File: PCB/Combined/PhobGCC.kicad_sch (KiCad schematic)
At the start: 74 parts, among them J2 Conn_01x04_Female, J3 Conn_01x01_Male, J4 Conn_01x04_Male, J5 Conn_01x02_Male, Q1 Q_NMOS_GSD, Q2 Q_PMOS_GDS, Q3 Q_NMOS_GSD, SW1 A, SW10 Dup, SW11 Dright, SW12 Ddown, SW2 B, SW3 X, SW4 Y, SW5 Start, SW6 L, SW7 R, SW9 Dleft, U1 Teensy4.0, U2 2x DRV5053CAQLPGM Hall Effect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, U3 GP2S60-MFG, U4 GP2S60-MFG, U5 Stickbox_Assembly

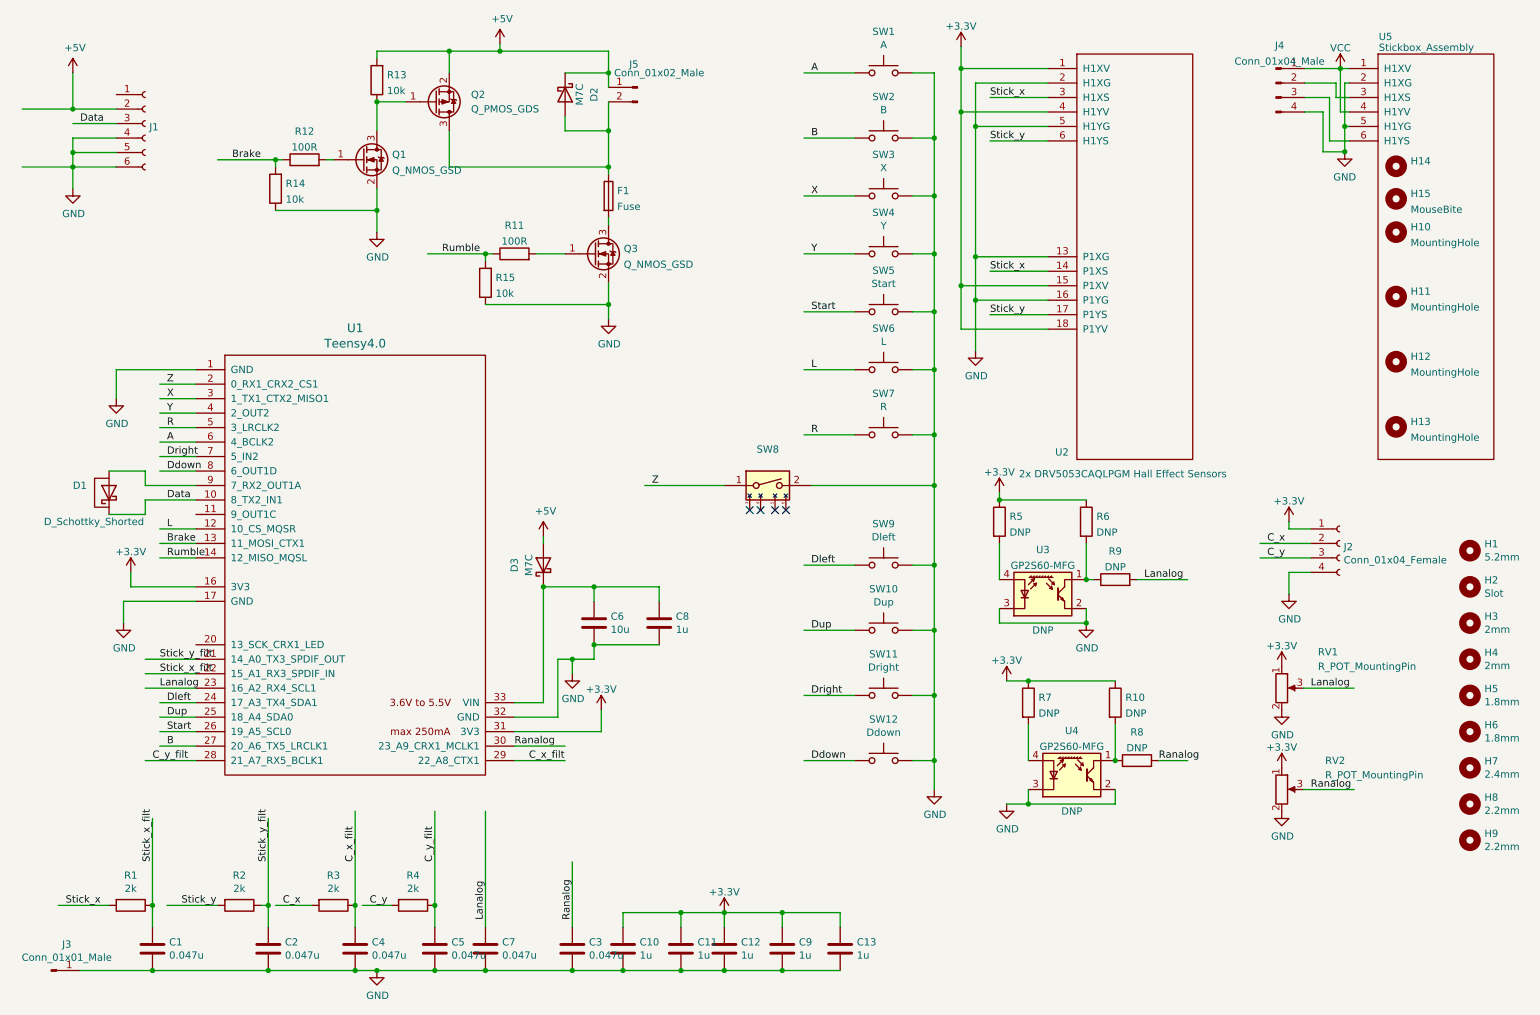
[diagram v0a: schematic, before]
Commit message: Rerouted the data signal to pin 7 of the teensy first, then to pin 8. This will allow the trace between pins 7 and 8 to be cut and a diode installed if the half-duplex communication needs to be reverted for some reason.
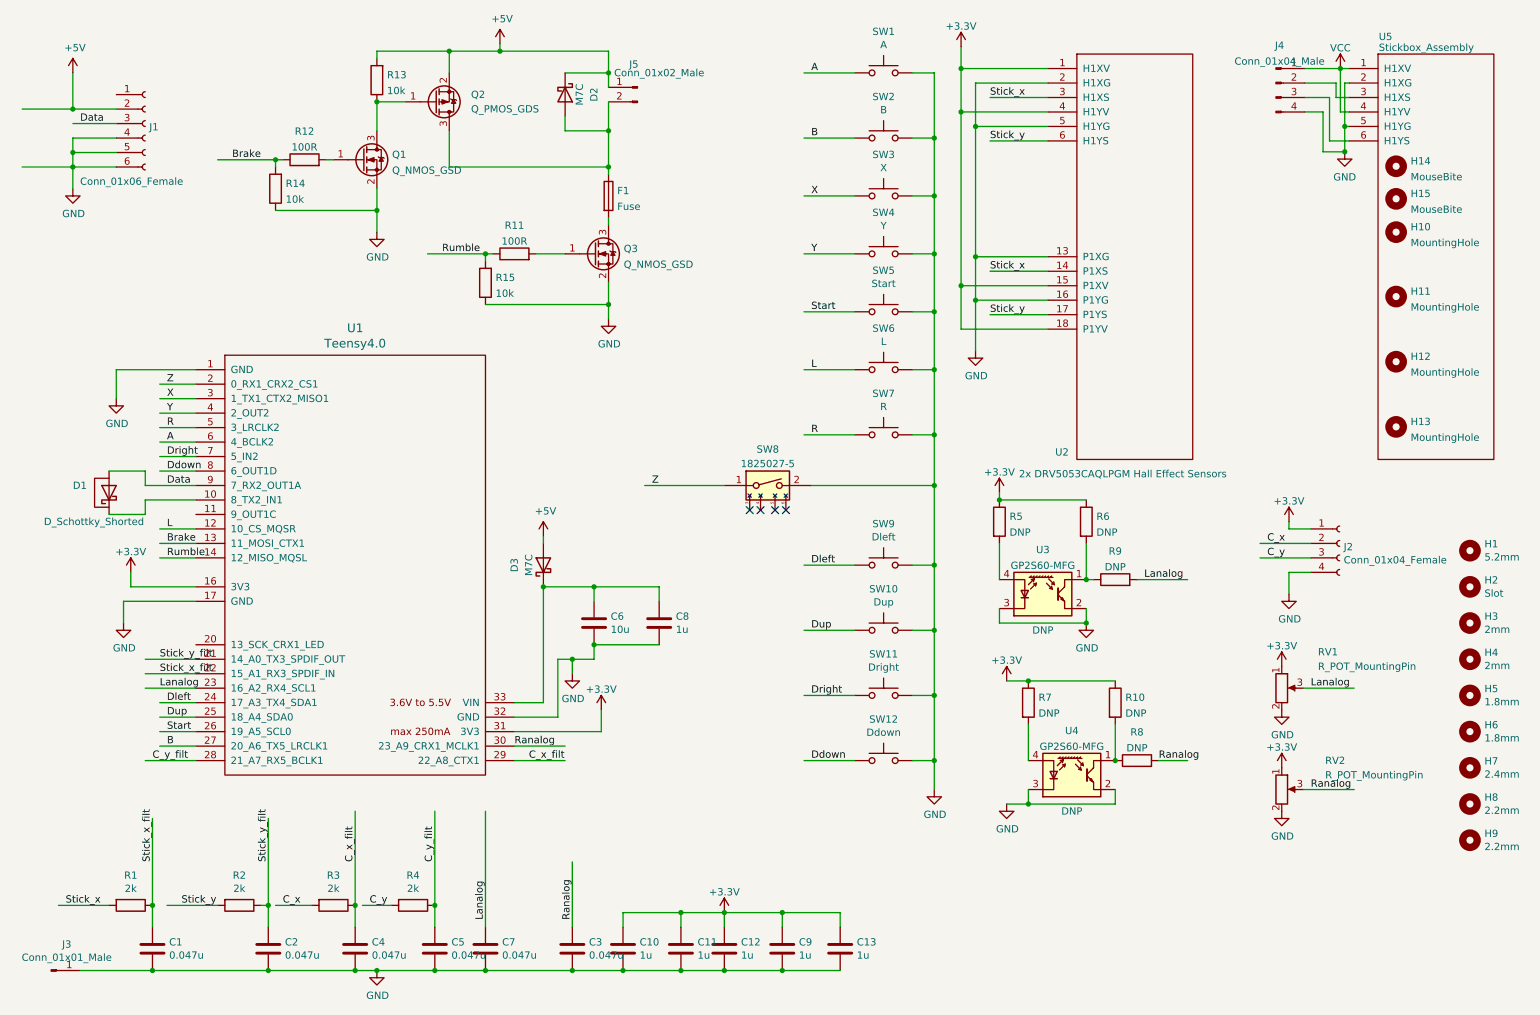
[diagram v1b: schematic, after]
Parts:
- H14: value (none) -> MouseBite; footprint (none) -> PhobGCC_Footprints:mouse-bite-2.54mm-slot
- H15: footprint (none) -> PhobGCC_Footprints:mouse-bite-2.54mm-slot
- J1: value (none) -> Conn_01x06_Female; footprint (none) -> PhobGCC_Footprints:GCC_Header_Straight_1x06_Pitch2.00mm
- SW8: value (none) -> 1825027-5; footprint (none) -> PhobGCC_Footprints:Z_Switch_Edge
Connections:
- net Data: now also D1.2 (A), U1.9 (7_RX2_OUT1A); no longer D1.1 (K), U1.10 (8_TX2_IN1)
- new net: D1.1 (K), U1.10 (8_TX2_IN1)
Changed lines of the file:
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@@
     (effects (font (size 1.27 1.27)) (justify left bottom))
   )
-  (label "Data" (at 43.18 97.79 0)
+  (label "Data" (at 43.18 95.25 0)
     (effects (font (size 1.27 1.27)) (justify left bottom))
   )
@@
       (effects (font (size 1.27 1.27)) (justify left))
     )
-    (property "Value" "" (id 1) (at 27.94 41.91 0)
-      (effects (font (size 1.27 1.27)) (justify left))
-    )
-    (property "Footprint" "" (id 2) (at 39.37 31.75 0)
+    (property "Value" "Conn_01x06_Female" (id 1) (at 27.94 41.91 0)
+      (effects (font (size 1.27 1.27)) (justify left))
+    )
+    (property "Footprint" "PhobGCC_Footprints:GCC_Header_Straight_1x06_Pitch2.00mm" (id 2) (at 39.37 31.75 0)
       (effects (font (size 1.27 1.27)) hide)
     )
@@
     (in_bom yes) (on_board yes)
     (property "Reference" "SW8" (id 0) (at 148.59 88.9 0))
-    (property "Value" "" (id 1) (at 148.59 91.44 0))
-    (property "Footprint" "" (id 2) (at 148.59 95.25 0)
+    (property "Value" "1825027-5" (id 1) (at 148.59 91.44 0))
+    (property "Footprint" "PhobGCC_Footprints:Z_Switch_Edge" (id 2) (at 148.59 95.25 0)
       (effects (font (size 1.27 1.27)) hide)
     )
@@
       (effects (font (size 1.27 1.27)) (justify left))
     )
-    (property "Value" "" (id 1) (at 261.366 41.1096 0)
-      (effects (font (size 1.27 1.27)) (justify left))
-    )
-    (property "Footprint" "" (id 2) (at 258.826 39.243 0)
+    (property "Value" "MouseBite" (id 1) (at 261.366 41.1096 0)
+      (effects (font (size 1.27 1.27)) (justify left))
+    )
+    (property "Footprint" "PhobGCC_Footprints:mouse-bite-2.54mm-slot" (id 2) (at 258.826 39.243 0)
       (effects (font (size 1.27 1.27)) hide)
     )
@@
       (effects (font (size 1.27 1.27)) (justify left))
     )
-    (property "Footprint" "" (id 2) (at 258.826 44.958 0)
-      (effects (font (size 1.27 1.27)) hide)
-    )
+    (property "Footprint" "PhobGCC_Footprints:mouse-bite-2.54mm-slot" (id 2) (at 258.826 44.958 0)
+      (effects (font (size 1.27 1.27)) hide)
+    )

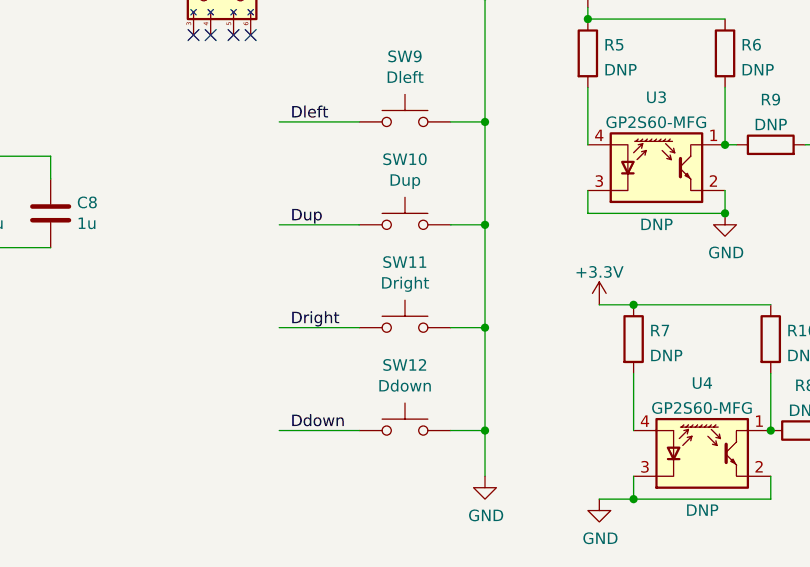
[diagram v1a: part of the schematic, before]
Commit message: fix dpad footprints
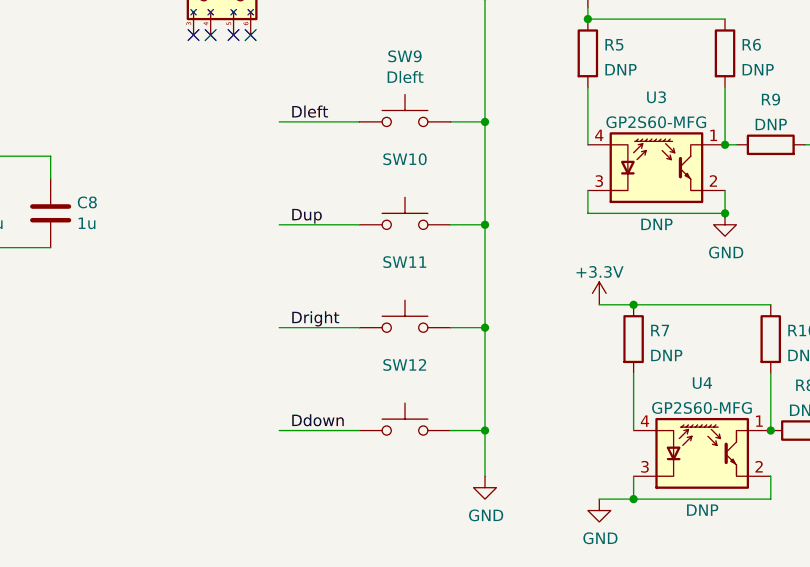
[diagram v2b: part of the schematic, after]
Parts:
- SW10: value Dup -> (none); footprint PhobGCC_Footprints:Dpad_Contact_TL3315NF_2 -> (none)
- SW11: value Dright -> (none); footprint PhobGCC_Footprints:Dpad_Contact_TL3315NF_2 -> (none)
- SW12: value Ddown -> (none); footprint PhobGCC_Footprints:Dpad_Contact_TL3315NF_2 -> (none)
- SW9: footprint PhobGCC_Footprints:Dpad_Contact_TL3315NF_2 -> (none)
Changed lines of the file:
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@@
     (property "Reference" "SW9" (id 0) (at 168.91 101.981 0))
     (property "Value" "Dleft" (id 1) (at 168.91 104.2924 0))
-    (property "Footprint" "PhobGCC_Footprints:Dpad_Contact_TL3315NF_2" (id 2) (at 168.91 104.14 0)
+    (property "Footprint" "" (id 2) (at 168.91 104.14 0)
       (effects (font (size 1.27 1.27)) hide)
     )
@@
     (in_bom yes) (on_board yes)
     (property "Reference" "SW10" (id 0) (at 168.91 113.411 0))
-    (property "Value" "Dup" (id 1) (at 168.91 115.7224 0))
-    (property "Footprint" "PhobGCC_Footprints:Dpad_Contact_TL3315NF_2" (id 2) (at 168.91 115.57 0)
+    (property "Value" "" (id 1) (at 168.91 115.7224 0))
+    (property "Footprint" "" (id 2) (at 168.91 115.57 0)
       (effects (font (size 1.27 1.27)) hide)
     )
@@
     (in_bom yes) (on_board yes)
     (property "Reference" "SW11" (id 0) (at 168.91 124.841 0))
-    (property "Value" "Dright" (id 1) (at 168.91 127.1524 0))
-    (property "Footprint" "PhobGCC_Footprints:Dpad_Contact_TL3315NF_2" (id 2) (at 168.91 127 0)
+    (property "Value" "" (id 1) (at 168.91 127.1524 0))
+    (property "Footprint" "" (id 2) (at 168.91 127 0)
       (effects (font (size 1.27 1.27)) hide)
     )
@@
     (in_bom yes) (on_board yes)
     (property "Reference" "SW12" (id 0) (at 168.91 136.271 0))
-    (property "Value" "Ddown" (id 1) (at 168.91 138.5824 0))
-    (property "Footprint" "PhobGCC_Footprints:Dpad_Contact_TL3315NF_2" (id 2) (at 168.91 138.43 0)
+    (property "Value" "" (id 1) (at 168.91 138.5824 0))
+    (property "Footprint" "" (id 2) (at 168.91 138.43 0)
       (effects (font (size 1.27 1.27)) hide)
     )
@@
     )
     (path "/00000000-0000-0000-0000-00006157aadd"
-      (reference "SW9") (unit 1) (value "Dleft") (footprint "PhobGCC_Footprints:Dpad_Contact_TL3315NF_2")
+      (reference "SW9") (unit 1) (value "Dleft") (footprint "PhobGCC_Footprints:Dpad_Contact_TL3315NF_3")
     )
     (path "/00000000-0000-0000-0000-00006157b24d"
-      (reference "SW10") (unit 1) (value "Dup") (footprint "PhobGCC_Footprints:Dpad_Contact_TL3315NF_2")
+      (reference "SW10") (unit 1) (value "Dup") (footprint "PhobGCC_Footprints:Dpad_Contact_TL3315NF_3")
     )
     (path "/00000000-0000-0000-0000-00006157b84b"
-      (reference "SW11") (unit 1) (value "Dright") (footprint "PhobGCC_Footprints:Dpad_Contact_TL3315NF_2")
+      (reference "SW11") (unit 1) (value "Dright") (footprint "PhobGCC_Footprints:Dpad_Contact_TL3315NF_3")
     )
     (path "/00000000-0000-0000-0000-00006157bdeb"
-      (reference "SW12") (unit 1) (value "Ddown") (footprint "PhobGCC_Footprints:Dpad_Contact_TL3315NF_2")
+      (reference "SW12") (unit 1) (value "Ddown") (footprint "PhobGCC_Footprints:Dpad_Contact_TL3315NF_3")
     )
     (path "/00000000-0000-0000-0000-00006154c933"

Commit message: schematic too
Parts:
- SW10: value (none) -> Dup; footprint (none) -> PhobGCC_Footprints:Dpad_Contact_TL3315NF_3
- SW11: value (none) -> Dright; footprint (none) -> PhobGCC_Footprints:Dpad_Contact_TL3315NF_3
- SW12: value (none) -> Ddown; footprint (none) -> PhobGCC_Footprints:Dpad_Contact_TL3315NF_3
- SW9: value Dleft -> (none)
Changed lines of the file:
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@@
     (in_bom yes) (on_board yes)
     (property "Reference" "SW9" (id 0) (at 168.91 101.981 0))
-    (property "Value" "Dleft" (id 1) (at 168.91 104.2924 0))
+    (property "Value" "" (id 1) (at 168.91 104.2924 0))
     (property "Footprint" "" (id 2) (at 168.91 104.14 0)
       (effects (font (size 1.27 1.27)) hide)
@@
     (in_bom yes) (on_board yes)
     (property "Reference" "SW10" (id 0) (at 168.91 113.411 0))
-    (property "Value" "" (id 1) (at 168.91 115.7224 0))
-    (property "Footprint" "" (id 2) (at 168.91 115.57 0)
+    (property "Value" "Dup" (id 1) (at 168.91 115.7224 0))
+    (property "Footprint" "PhobGCC_Footprints:Dpad_Contact_TL3315NF_3" (id 2) (at 168.91 115.57 0)
       (effects (font (size 1.27 1.27)) hide)
     )
@@
     (in_bom yes) (on_board yes)
     (property "Reference" "SW11" (id 0) (at 168.91 124.841 0))
-    (property "Value" "" (id 1) (at 168.91 127.1524 0))
-    (property "Footprint" "" (id 2) (at 168.91 127 0)
+    (property "Value" "Dright" (id 1) (at 168.91 127.1524 0))
+    (property "Footprint" "PhobGCC_Footprints:Dpad_Contact_TL3315NF_3" (id 2) (at 168.91 127 0)
       (effects (font (size 1.27 1.27)) hide)
     )
@@
     (in_bom yes) (on_board yes)
     (property "Reference" "SW12" (id 0) (at 168.91 136.271 0))
-    (property "Value" "" (id 1) (at 168.91 138.5824 0))
-    (property "Footprint" "" (id 2) (at 168.91 138.43 0)
+    (property "Value" "Ddown" (id 1) (at 168.91 138.5824 0))
+    (property "Footprint" "PhobGCC_Footprints:Dpad_Contact_TL3315NF_3" (id 2) (at 168.91 138.43 0)
       (effects (font (size 1.27 1.27)) hide)
     )
